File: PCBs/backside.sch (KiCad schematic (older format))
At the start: 45 parts, among them J1 9Pin, J3 Power, J5 Matrix, J7 Driver output 2, J9 Driver output 1, U1 HT1632C-52LQFP, U2 HT1632C-52LQFP, U3 STM32F103C8T6

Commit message: Finished routing, updated comm channel displays
Decided to use (and again modify) open hornet's com channel indicators. Finished routing traces and adding ground planes on the main board, though it may be a little sloppy. Began work on the back side board, which will have the LED drivers and STM32. Re added the shift register board for now for the sake of having more pins.
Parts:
- removed J9: Driver output 1, Connector_PinSocket_2.54mm:PinSocket_1x33_P2.54mm_Vertical, symbol Connector:Conn_01x33_Male
- added A1: ShiftRegisterBoard, UFC:ShiftRegisterBoardPins, symbol UFClib:ShiftRegisterBoard
- added C10, C3, C4, C5, C6, C7, C8, C9: .1uF, Capacitor_SMD:C_0603_1608Metric_Pad1.08x0.95mm_HandSolder, symbol Device:C
- added J10, J12: Conn_01x08_Male, Connector_PinSocket_2.54mm:PinSocket_1x08_P2.54mm_Vertical, symbol Connector:Conn_01x08_Male
- added J11, J13: Conn_01x09_Male, Connector_PinSocket_2.54mm:PinSocket_1x09_P2.54mm_Vertical, symbol Connector:Conn_01x09_Male
- added J14, J15, J16: Conn_01x07_Male, Connector_PinSocket_2.54mm:PinSocket_1x07_P2.54mm_Vertical, symbol Connector:Conn_01x07_Male
- added J17, J8: Conn_01x04_Male, Connector_PinSocket_2.54mm:PinSocket_1x04_P2.54mm_Vertical, symbol Connector:Conn_01x04_Male
- added J4, J6: Conn_01x17_Male, Connector_PinSocket_2.54mm:PinSocket_1x17_P2.54mm_Vertical, symbol Connector:Conn_01x17_Male
- added J9: Conn_01x30_Male, Connector_PinSocket_2.54mm:PinSocket_1x30_P2.54mm_Vertical, symbol Connector:Conn_01x30_Male
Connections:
- net labels added: Analog1, Analog2, Analog3, Analog4, Analog5, Analog6, Analog7, DIN1, DIN10, DIN11, DIN12, DIN13, DIN14, DIN15, DIN16, DIN17, DIN2, DIN3, DIN4, DIN5, DIN6, DIN7, DIN8, DIN9, DigInt1, DigInt2, DigInt3, DigInt4, SRCLK, SRCS, SRMISO
- wire segments 186 -> 188
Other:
- note added: "Analog input filtering (optional)"
- note added: "Break out unused input pins, with ground"
- note added: "Left comm\n"
- note added: "Right comm"
- moved on the sheet: J1, J3, J5, J7, R35, U1

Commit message: Routed back side board
Routed the LED drivers, pin headers, shift registers, etc. that are on the back side. ECAD is close to done, and I will start on the MCAD at this point.
-Decided to avoid routing anodes and common cathodes to each of the comm channel displays, as that would probably have required at least an extra layer, instead I added a header to plug crimped wires directly into the front side.
-Some of the headers are two single width pin headers put side by side, meaning their courtyards overlap. I may redo this to use one footprint for both in the future.
-Still undecided on a couple part values
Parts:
- added J18: Conn_02x17_Odd_Even, Connector_PinSocket_2.54mm:PinSocket_2x17_P2.54mm_Vertical, symbol Connector_Generic:Conn_02x17_Odd_Even

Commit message: Updated silkscreen, fixed minor issues
Updated silkscreen to include pin designations, and fixed minor issue with ground plane
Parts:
- R1, R10, R11, R12, R13, R14, R15, R16, R17, R18, R19, R2, R20, R21, R22, R23, R24, R25, R26, R27, R28, R29, R3, R30, R31, R32, R33, R34, R4, R5, R6, R7, R8, R9: value 520R -> 510R
- R35: value ? -> 100R

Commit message: Removed comm displays from PCB
Since they will be connected with wires anyways it didn't make sense to keep them on.
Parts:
- removed J10, J12: Conn_01x08_Male, Connector_PinSocket_2.54mm:PinSocket_1x08_P2.54mm_Vertical, symbol Connector:Conn_01x08_Male
- removed J11, J13: Conn_01x09_Male, Connector_PinSocket_2.54mm:PinSocket_1x09_P2.54mm_Vertical, symbol Connector:Conn_01x09_Male
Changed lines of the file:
@@
 $Descr A4 11693 8268
 encoding utf-8
-Sheet 1 1
+Sheet 3 3
 Title ""
 Date ""
@@
 Text Label 9200 3600 2    50   ~ 0
 DATA
-$Comp
-L Connector:Conn_01x09_Male J11
-U 1 1 60A3F5DA
-P 1800 7150
-F 0 "J11" H 1908 7731 50  0000 C CNN
-F 1 "Conn_01x09_Male" H 1908 7640 50  0000 C CNN
-F 2 "Connector_PinSocket_2.54mm:PinSocket_1x09_P2.54mm_Vertical" H 1800 7150 50  0001 C CNN
-F 3 "~" H 1800 7150 50  0001 C CNN
-	1    1800 7150
-	1    0    0    -1
-$EndComp
-Text Notes 1350 6450 0    50   ~ 0
+Text Notes 2350 7450 0    50   ~ 0
 Left comm\n
-Text Notes 5100 6450 0    50   ~ 0
+Text Notes 3850 7450 0    50   ~ 0
 Right comm
 $Comp
-L Connector:Conn_01x08_Male J10
-U 1 1 60A85603
-P 1150 7150
-F 0 "J10" H 1258 7631 50  0000 C CNN
-F 1 "Conn_01x08_Male" H 1258 7540 50  0000 C CNN
-F 2 "Connector_PinSocket_2.54mm:PinSocket_1x08_P2.54mm_Vertical" H 1150 7150 50  0001 C CNN
-F 3 "~" H 1150 7150 50  0001 C CNN
-	1    1150 7150
-	1    0    0    -1
-$EndComp
-Text Label 1350 6850 0    50   ~ 0
-J1
-Text Label 1350 6950 0    50   ~ 0
-K1
-Text Label 1350 7050 0    50   ~ 0
-L1
-Text Label 1350 7150 0    50   ~ 0
-M1
-Text Label 1350 7250 0    50   ~ 0
-N1
-Text Label 1350 7350 0    50   ~ 0
-P1
-Text Label 1350 7450 0    50   ~ 0
-Q1
-Text Label 1350 7550 0    50   ~ 0
-DP1
-Text Label 2000 6750 0    50   ~ 0
-COM13-1
-Text Label 2000 6850 0    50   ~ 0
-A1
-Text Label 2000 6950 0    50   ~ 0
-B1
-Text Label 2000 7050 0    50   ~ 0
-C1
-Text Label 2000 7150 0    50   ~ 0
-D1
-Text Label 2000 7250 0    50   ~ 0
-E1
-Text Label 2000 7350 0    50   ~ 0
-F1
-Text Label 2000 7450 0    50   ~ 0
-G1
-Text Label 2000 7550 0    50   ~ 0
-H1
-$Comp
-L Connector:Conn_01x09_Male J13
-U 1 1 60ACB9DE
-P 5500 7150
-F 0 "J13" H 5608 7731 50  0000 C CNN
-F 1 "Conn_01x09_Male" H 5608 7640 50  0000 C CNN
-F 2 "Connector_PinSocket_2.54mm:PinSocket_1x09_P2.54mm_Vertical" H 5500 7150 50  0001 C CNN
-F 3 "~" H 5500 7150 50  0001 C CNN
-	1    5500 7150
-	1    0    0    -1
-$EndComp
-$Comp
-L Connector:Conn_01x08_Male J12
-U 1 1 60ACB9E4
-P 4850 7150
-F 0 "J12" H 4958 7631 50  0000 C CNN
-F 1 "Conn_01x08_Male" H 4958 7540 50  0000 C CNN
-F 2 "Connector_PinSocket_2.54mm:PinSocket_1x08_P2.54mm_Vertical" H 4850 7150 50  0001 C CNN
-F 3 "~" H 4850 7150 50  0001 C CNN
-	1    4850 7150
-	1    0    0    -1
-$EndComp
-Text Label 5050 6850 0    50   ~ 0
-J1
-Text Label 5050 6950 0    50   ~ 0
-K1
-Text Label 5050 7050 0    50   ~ 0
-L1
-Text Label 5050 7150 0    50   ~ 0
-M1
-Text Label 5050 7250 0    50   ~ 0
-N1
-Text Label 5050 7350 0    50   ~ 0
-P1
-Text Label 5050 7450 0    50   ~ 0
-Q1
-Text Label 5050 7550 0    50   ~ 0
-DP1
-Text Label 5700 6750 0    50   ~ 0
-COM14-1
-Text Label 5700 6850 0    50   ~ 0
-A1
-Text Label 5700 6950 0    50   ~ 0
-B1
-Text Label 5700 7050 0    50   ~ 0
-C1
-Text Label 5700 7150 0    50   ~ 0
-D1
-Text Label 5700 7250 0    50   ~ 0
-E1
-Text Label 5700 7350 0    50   ~ 0
-F1
-Text Label 5700 7450 0    50   ~ 0
-G1
-Text Label 5700 7550 0    50   ~ 0
-H1
-$Comp
 L Connector:Conn_01x30_Male J9

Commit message: Updated PCBs, cleaned up files
No commit for a while; a lot has happened in the mean time. JLC refused my order for the display layers, so I settled for just the dot layer. The gerbers for the rest are deleted, but the kicad files are still present.

I also received the main PCBs from JLC, and edited a couple small details.
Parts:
- R1, R10, R11, R12, R13, R14, R15, R16, R17, R18, R19, R2, R20, R21, R22, R23, R24, R25, R26, R27, R28, R29, R3, R30, R31, R32, R33, R34, R35, R4, R5, R6, R7, R8, R9: footprint Resistor_SMD:R_1206_3216Metric -> Resistor_SMD:R_1206_3216Metric_Pad1.30x1.75mm_HandSolder

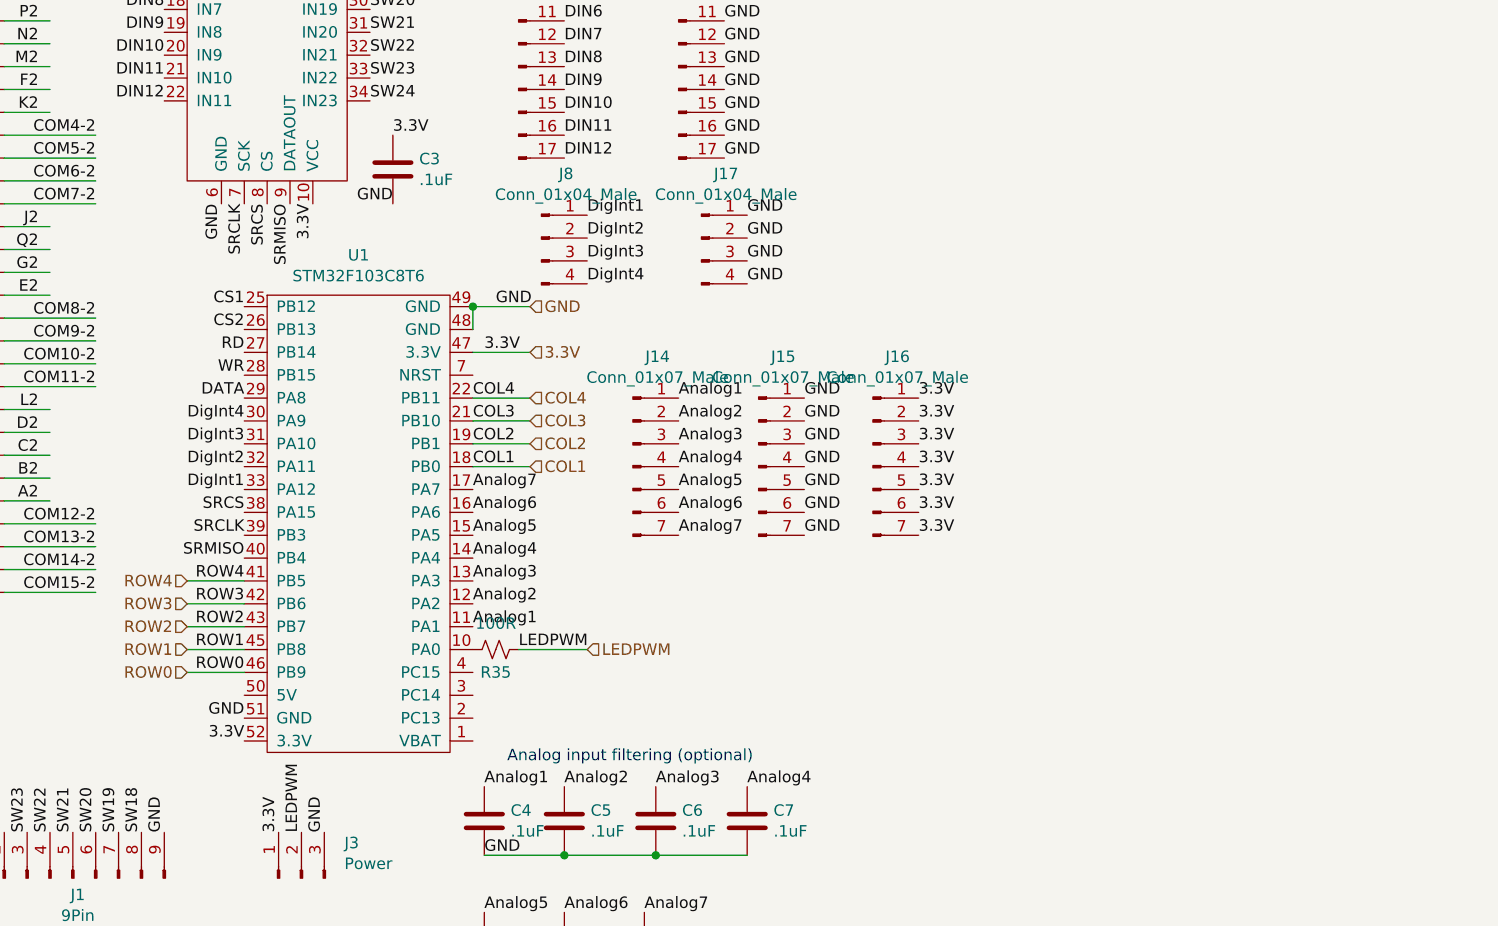
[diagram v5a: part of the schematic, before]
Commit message: Fixed design error
Untested as of now.
Removed direct connection from PWM out to LEDs, as the PWM pins on the bluepill can't provide enough current. Added P channel mosfet, and individual resistors per parallel LED. For now, the single resistor for all LEDs is still present, but bypassable via jumper, for the sake of backwards compatibility.
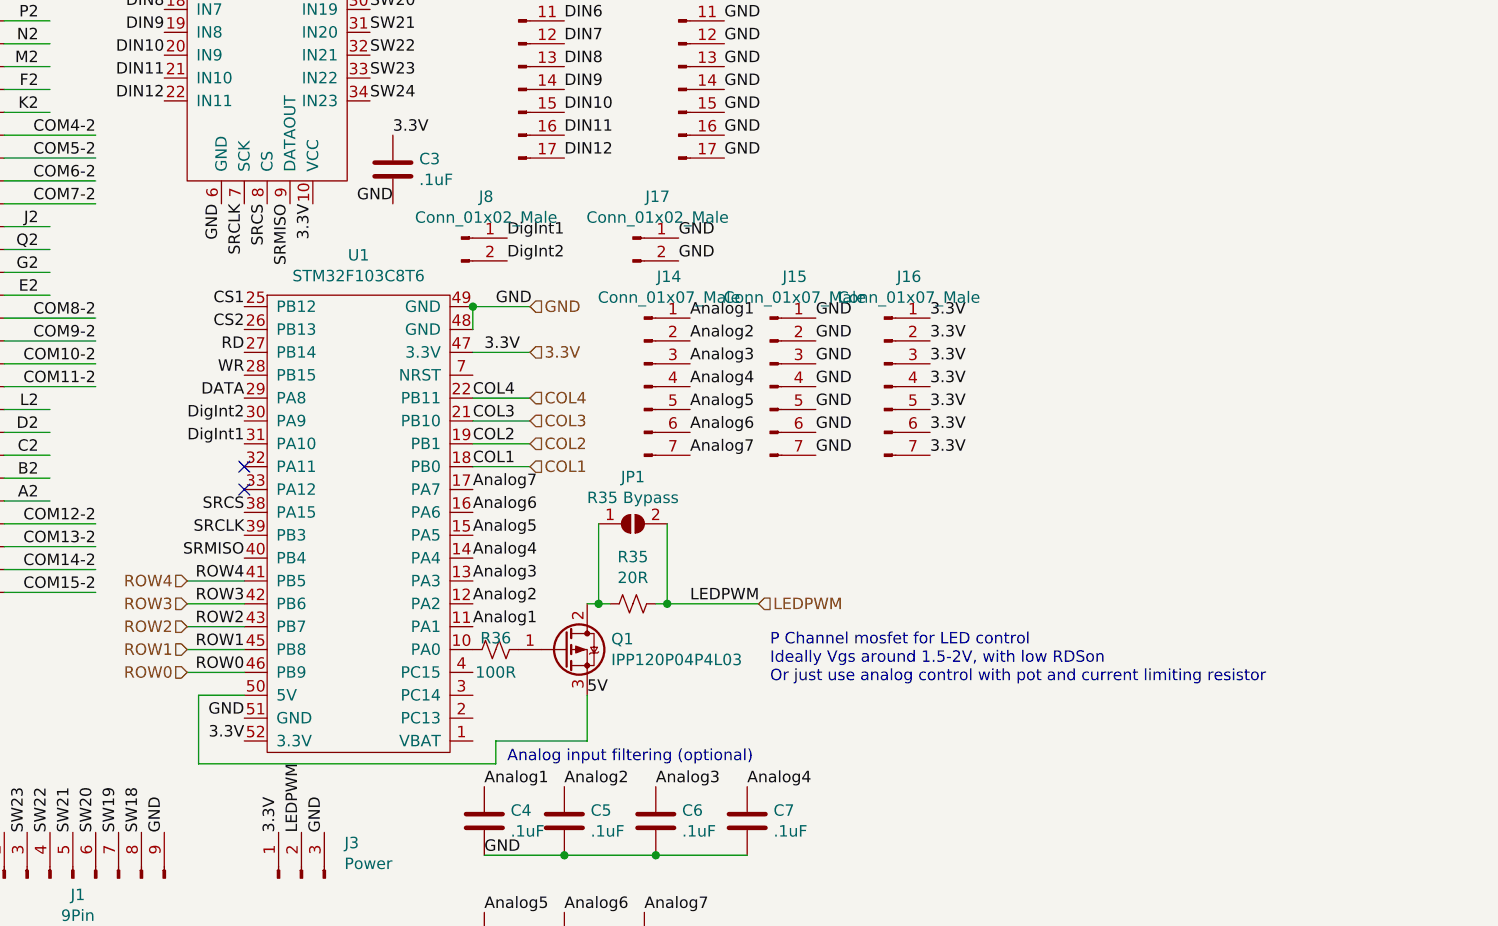
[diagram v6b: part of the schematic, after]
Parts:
- removed J17, J8: Conn_01x04_Male, Connector_PinSocket_2.54mm:PinSocket_1x04_P2.54mm_Vertical, symbol Connector:Conn_01x04_Male
- added J17, J8: Conn_01x02_Male, Connector_PinSocket_2.54mm:PinSocket_1x02_P2.54mm_Vertical, symbol Connector:Conn_01x02_Male
- added JP1: R35 Bypass, Jumper:SolderJumper-2_P1.3mm_Open_Pad1.0x1.5mm, symbol Jumper:SolderJumper_2_Open
- added Q1: IPP120P04P4L03, Package_TO_SOT_THT:TO-220-3_Vertical, symbol Transistor_FET:IRF4905
- added R36: 100R, Resistor_SMD:R_1206_3216Metric_Pad1.30x1.75mm_HandSolder, symbol Device:R_Small_US
- R35: value 100R -> 20R
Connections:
- net labels added: 5V
- net labels removed: DigInt3, DigInt4
- wire segments 188 -> 199
- no-connect marks 0 -> 2
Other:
- note added: "P Channel mosfet for LED control\nIdeally Vgs around 1.5-2V, with low RDSon\nOr just use analog control with pot and current limiting resistor"
- moved on the sheet: J14, J15, J16
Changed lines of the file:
@@
 Text Label 8150 5500 1    50   ~ 0
 SW24
-Text Label 10400 4700 0    50   ~ 0
+Text Label 11150 4500 0    50   ~ 0
 LEDPWM
-$Comp
-L Device:R_Small_US R35
-U 1 1 6125D469
-P 10300 4700
-AR Path="/6125D469" Ref="R35"  Part="1"
-AR Path="/60CB907D/6125D469" Ref="R35"  Part="1"
-F 0 "R35" V 10400 4700 50  0000 C CNN
-F 1 "100R" V 10186 4700 50  0000 C CNN
-F 2 "Resistor_SMD:R_1206_3216Metric_Pad1.30x1.75mm_HandSolder" H 10300 4700 50  0001 C CNN
-F 3 "~" H 10300 4700 50  0001 C CNN
-	1    10300 4700
-	0    1    1    0
-$EndComp
 $Comp
 L Connector:Conn_01x09_Male J1
@@
 Wire Wire Line
 	9200 4400 8950 4400
-Wire Wire Line
-	10400 4700 10700 4700
-Text HLabel 10700 4700 2    50   Input ~ 0
+Text HLabel 11450 4500 2    50   Input ~ 0
 LEDPWM
 Text HLabel 8950 4500 0    50   Input ~ 0
@@
 Text Label 10200 4000 0    50   ~ 0
 Analog7
-Text Label 9200 4000 2    50   ~ 0
+Text Label 9200 3800 2    50   ~ 0
 DigInt1
-Text Label 9200 3900 2    50   ~ 0
+Text Label 9200 3700 2    50   ~ 0
 DigInt2
-Text Label 9200 3800 2    50   ~ 0
-DigInt3
-Text Label 9200 3700 2    50   ~ 0
-DigInt4
 Text Label 9100 750  1    50   ~ 0
 GND
@@
 Text Label 11300 2550 0    50   ~ 0
 GND
-$Comp
-L Connector:Conn_01x04_Male J8
-U 1 1 60DADE95
-P 10500 2900
-F 0 "J8" H 10608 3181 50  0000 C CNN
-F 1 "Conn_01x04_Male" H 10608 3090 50  0000 C CNN
-F 2 "Connector_PinSocket_2.54mm:PinSocket_1x04_P2.54mm_Vertical" H 10500 2900 50  0001 C CNN
-F 3 "~" H 10500 2900 50  0001 C CNN
-	1    10500 2900
-	1    0    0    -1
-$EndComp
-$Comp
-L Connector:Conn_01x04_Male J17
-U 1 1 60DAEEA9
-P 11200 2900
-F 0 "J17" H 11308 3181 50  0000 C CNN
-F 1 "Conn_01x04_Male" H 11308 3090 50  0000 C CNN
-F 2 "Connector_PinSocket_2.54mm:PinSocket_1x04_P2.54mm_Vertical" H 11200 2900 50  0001 C CNN
-F 3 "~" H 11200 2900 50  0001 C CNN
-	1    11200 2900
-	1    0    0    -1
-$EndComp
-Text Label 10700 2800 0    50   ~ 0
-DigInt1
-Text Label 10700 2900 0    50   ~ 0
-DigInt2
-Text Label 10700 3000 0    50   ~ 0
-DigInt3
-Text Label 10700 3100 0    50   ~ 0
-DigInt4
-Text Label 11400 2800 0    50   ~ 0
-GND
-Text Label 11400 2900 0    50   ~ 0
-GND
-Text Label 11400 3000 0    50   ~ 0
-GND
-Text Label 11400 3100 0    50   ~ 0
+Text Label 11100 2900 0    50   ~ 0
+GND
+Text Label 11100 3000 0    50   ~ 0
 GND
 $Comp
 L Connector:Conn_01x07_Male J14
 U 1 1 60E0E0E7
-P 10900 3900
-F 0 "J14" H 11008 4381 50  0000 C CNN
-F 1 "Conn_01x07_Male" H 11008 4290 50  0000 C CNN
-F 2 "Connector_PinSocket_2.54mm:PinSocket_1x07_P2.54mm_Vertical" H 10900 3900 50  0001 C CNN
-F 3 "~" H 10900 3900 50  0001 C CNN
-	1    10900 3900
+P 10950 3550
+F 0 "J14" H 11058 4031 50  0000 C CNN
+F 1 "Conn_01x07_Male" H 11058 3940 50  0000 C CNN
+F 2 "Connector_PinSocket_2.54mm:PinSocket_1x07_P2.54mm_Vertical" H 10950 3550 50  0001 C CNN
+F 3 "~" H 10950 3550 50  0001 C CNN
+	1    10950 3550
 	1    0    0    -1
 $EndComp
@@
 L Connector:Conn_01x07_Male J15
 U 1 1 60E0F8D9
-P 11450 3900
-F 0 "J15" H 11558 4381 50  0000 C CNN
-F 1 "Conn_01x07_Male" H 11558 4290 50  0000 C CNN
-F 2 "Connector_PinSocket_2.54mm:PinSocket_1x07_P2.54mm_Vertical" H 11450 3900 50  0001 C CNN
-F 3 "~" H 11450 3900 50  0001 C CNN
-	1    11450 3900
+P 11500 3550
+F 0 "J15" H 11608 4031 50  0000 C CNN
+F 1 "Conn_01x07_Male" H 11608 3940 50  0000 C CNN
+F 2 "Connector_PinSocket_2.54mm:PinSocket_1x07_P2.54mm_Vertical" H 11500 3550 50  0001 C CNN
+F 3 "~" H 11500 3550 50  0001 C CNN
+	1    11500 3550
 	1    0    0    -1
 $EndComp
@@
 L Connector:Conn_01x07_Male J16
 U 1 1 60E1F3DE
-P 11950 3900
-F 0 "J16" H 12058 4381 50  0000 C CNN
-F 1 "Conn_01x07_Male" H 12058 4290 50  0000 C CNN
-F 2 "Connector_PinSocket_2.54mm:PinSocket_1x07_P2.54mm_Vertical" H 11950 3900 50  0001 C CNN
-F 3 "~" H 11950 3900 50  0001 C CNN
-	1    11950 3900
-	1    0    0    -1
-$EndComp
-Text Label 11100 3600 0    50   ~ 0
+P 12000 3550
+F 0 "J16" H 12108 4031 50  0000 C CNN
+F 1 "Conn_01x07_Male" H 12108 3940 50  0000 C CNN
+F 2 "Connector_PinSocket_2.54mm:PinSocket_1x07_P2.54mm_Vertical" H 12000 3550 50  0001 C CNN
+F 3 "~" H 12000 3550 50  0001 C CNN
+	1    12000 3550
+	1    0    0    -1
+$EndComp
+Text Label 11150 3250 0    50   ~ 0
 Analog1
-Text Label 11100 3700 0    50   ~ 0
+Text Label 11150 3350 0    50   ~ 0
 Analog2
-Text Label 11100 3800 0    50   ~ 0
+Text Label 11150 3450 0    50   ~ 0
 Analog3
-Text Label 11100 3900 0    50   ~ 0
+Text Label 11150 3550 0    50   ~ 0
 Analog4
-Text Label 11100 4000 0    50   ~ 0
+Text Label 11150 3650 0    50   ~ 0
 Analog5
-Text Label 11100 4100 0    50   ~ 0
+Text Label 11150 3750 0    50   ~ 0
 Analog6
-Text Label 11100 4200 0    50   ~ 0
+Text Label 11150 3850 0    50   ~ 0
 Analog7
-Text Label 11650 3600 0    50   ~ 0
-GND
-Text Label 11650 3700 0    50   ~ 0
-GND
-Text Label 11650 3800 0    50   ~ 0
-GND
-Text Label 11650 3900 0    50   ~ 0
-GND
-Text Label 11650 4000 0    50   ~ 0
-GND
-Text Label 11650 4100 0    50   ~ 0
-GND
-Text Label 11650 4200 0    50   ~ 0
-GND
-Text Label 12150 3600 0    50   ~ 0
-3.3V
-Text Label 12150 3700 0    50   ~ 0
-3.3V
-Text Label 12150 3800 0    50   ~ 0
-3.3V
-Text Label 12150 3900 0    50   ~ 0
-3.3V
-Text Label 12150 4000 0    50   ~ 0
-3.3V
-Text Label 12150 4100 0    50   ~ 0
-3.3V
-Text Label 12150 4200 0    50   ~ 0
+Text Label 11700 3250 0    50   ~ 0
+GND
+Text Label 11700 3350 0    50   ~ 0
+GND
+Text Label 11700 3450 0    50   ~ 0
+GND
+Text Label 11700 3550 0    50   ~ 0
+GND
+Text Label 11700 3650 0    50   ~ 0
+GND
+Text Label 11700 3750 0    50   ~ 0
+GND
+Text Label 11700 3850 0    50   ~ 0
+GND
+Text Label 12200 3250 0    50   ~ 0
+3.3V
+Text Label 12200 3350 0    50   ~ 0
+3.3V
+Text Label 12200 3450 0    50   ~ 0
+3.3V
+Text Label 12200 3550 0    50   ~ 0
+3.3V
+Text Label 12200 3650 0    50   ~ 0
+3.3V
+Text Label 12200 3750 0    50   ~ 0
+3.3V
+Text Label 12200 3850 0    50   ~ 0
 3.3V
 Text Notes 10250 700  0    50   ~ 0
@@
 Text Label 3100 8400 2    50   ~ 0
 DP1
+NoConn ~ 9200 3900
+NoConn ~ 9200 4000
+$Comp
+L Connector:Conn_01x02_Male J8
+U 1 1 60C4B228
+P 10150 2900
+F 0 "J8" H 10258 3081 50  0000 C CNN
+F 1 "Conn_01x02_Male" H 10258 2990 50  0000 C CNN
+F 2 "Connector_PinSocket_2.54mm:PinSocket_1x02_P2.54mm_Vertical" H 10150 2900 50  0001 C CNN
+F 3 "~" H 10150 2900 50  0001 C CNN
+	1    10150 2900
+	1    0    0    -1
+$EndComp
+Text Label 10350 3000 0    50   ~ 0
+DigInt2
+Text Label 10350 2900 0    50   ~ 0
+DigInt1
+Wire Wire Line
+	10300 5100 10300 5200
+Wire Wire Line
+	10300 5200 9000 5200
+Wire Wire Line
+	9000 5200 9000 4900
+Wire Wire Line
+	9000 4900 9200 4900
+Text Label 10700 4900 0    50   ~ 0
+5V
+Text Notes 11500 4850 0    50   ~ 0
+P Channel mosfet for LED control\nIdeally Vgs around 1.5-2V, with low RDSon\nOr just use analog control with pot and current limiting resistor
+$Comp
+L Device:R_Small_US R35
+U 1 1 60CAD7D0
+P 10900 4500
+F 0 "R35" V 10695 4500 50  0000 C CNN
+F 1 "20R" V 10786 4500 50  0000 C CNN
+F 2 "Resistor_SMD:R_1206_3216Metric_Pad1.30x1.75mm_HandSolder" H 10900 4500 50  0001 C CNN
+F 3 "~" H 10900 4500 50  0001 C CNN
+	1    10900 4500
+	0    1    1    0
+$EndComp
+Wire Wire Line
+	11000 4500 11050 4500
+$Comp
+L Device:R_Small_US R36
+U 1 1 60CD2B90
+P 10300 4700
+F 0 "R36" V 10250 4700 50  0000 C CNN
+F 1 "100R" V 10400 4700 50  0000 C CNN
+F 2 "Resistor_SMD:R_1206_3216Metric_Pad1.30x1.75mm_HandSolder" H 10300 4700 50  0001 C CNN
+F 3 "~" H 10300 4700 50  0001 C CNN
+	1    10300 4700
+	0    1    1    0
+$EndComp
+Wire Wire Line
+	10700 4500 10750 4500
+Wire Wire Line
+	10700 5100 10700 4900
+Wire Wire Line
+	10300 5100 10700 5100
+$Comp
+L Connector:Conn_01x02_Male J17
+U 1 1 60D6BD85
+P 10900 2900
+F 0 "J17" H 11008 3081 50  0000 C CNN
+F 1 "Conn_01x02_Male" H 11008 2990 50  0000 C CNN
+F 2 "Connector_PinSocket_2.54mm:PinSocket_1x02_P2.54mm_Vertical" H 10900 2900 50  0001 C CNN
+F 3 "~" H 10900 2900 50  0001 C CNN
+	1    10900 2900
+	1    0    0    -1
+$EndComp
+$Comp
+L Jumper:SolderJumper_2_Open JP1
+U 1 1 60C47DC2
+P 10900 4150
+F 0 "JP1" H 10900 4355 50  0000 C CNN
+F 1 "R35 Bypass" H 10900 4264 50  0000 C CNN
+F 2 "Jumper:SolderJumper-2_P1.3mm_Open_Pad1.0x1.5mm" H 10900 4150 50  0001 C CNN
+F 3 "~" H 10900 4150 50  0001 C CNN
+	1    10900 4150
+	1    0    0    -1
+$EndComp
+Wire Wire Line
+	10750 4150 10750 4500
+Connection ~ 10750 4500
+Wire Wire Line
+	10750 4500 10800 4500
+Wire Wire Line
+	11050 4150 11050 4500
+Connection ~ 11050 4500
+Wire Wire Line
+	11050 4500 11450 4500
+$Comp
+L Transistor_FET:IRF4905 Q1
+U 1 1 60CE45B5
+P 10600 4700
+F 0 "Q1" H 10805 4746 50  0000 L CNN
+F 1 "IPP120P04P4L03" H 10805 4655 50  0000 L CNN
+F 2 "Package_TO_SOT_THT:TO-220-3_Vertical" H 10800 4625 50  0001 L CIN
+F 3 "http://www.infineon.com/dgdl/irf4905.pdf?fileId=5546d462533600a4015355e32165197c" H 10600 4700 50  0001 L CNN
+	1    10600 4700
+	1    0    0    -1
+$EndComp
 $EndSCHEMATC
